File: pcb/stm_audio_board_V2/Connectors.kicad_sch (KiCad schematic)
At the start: 12 parts, among them J1 Power conn, J2 STlink, J3 Audio_sig, J4 Conn_01x10_display, J4 Conn_01x10_pots_internal, J5 SPI, J6 Conn_01x03_pot_ext, J6 Conn_01x03_taptempo

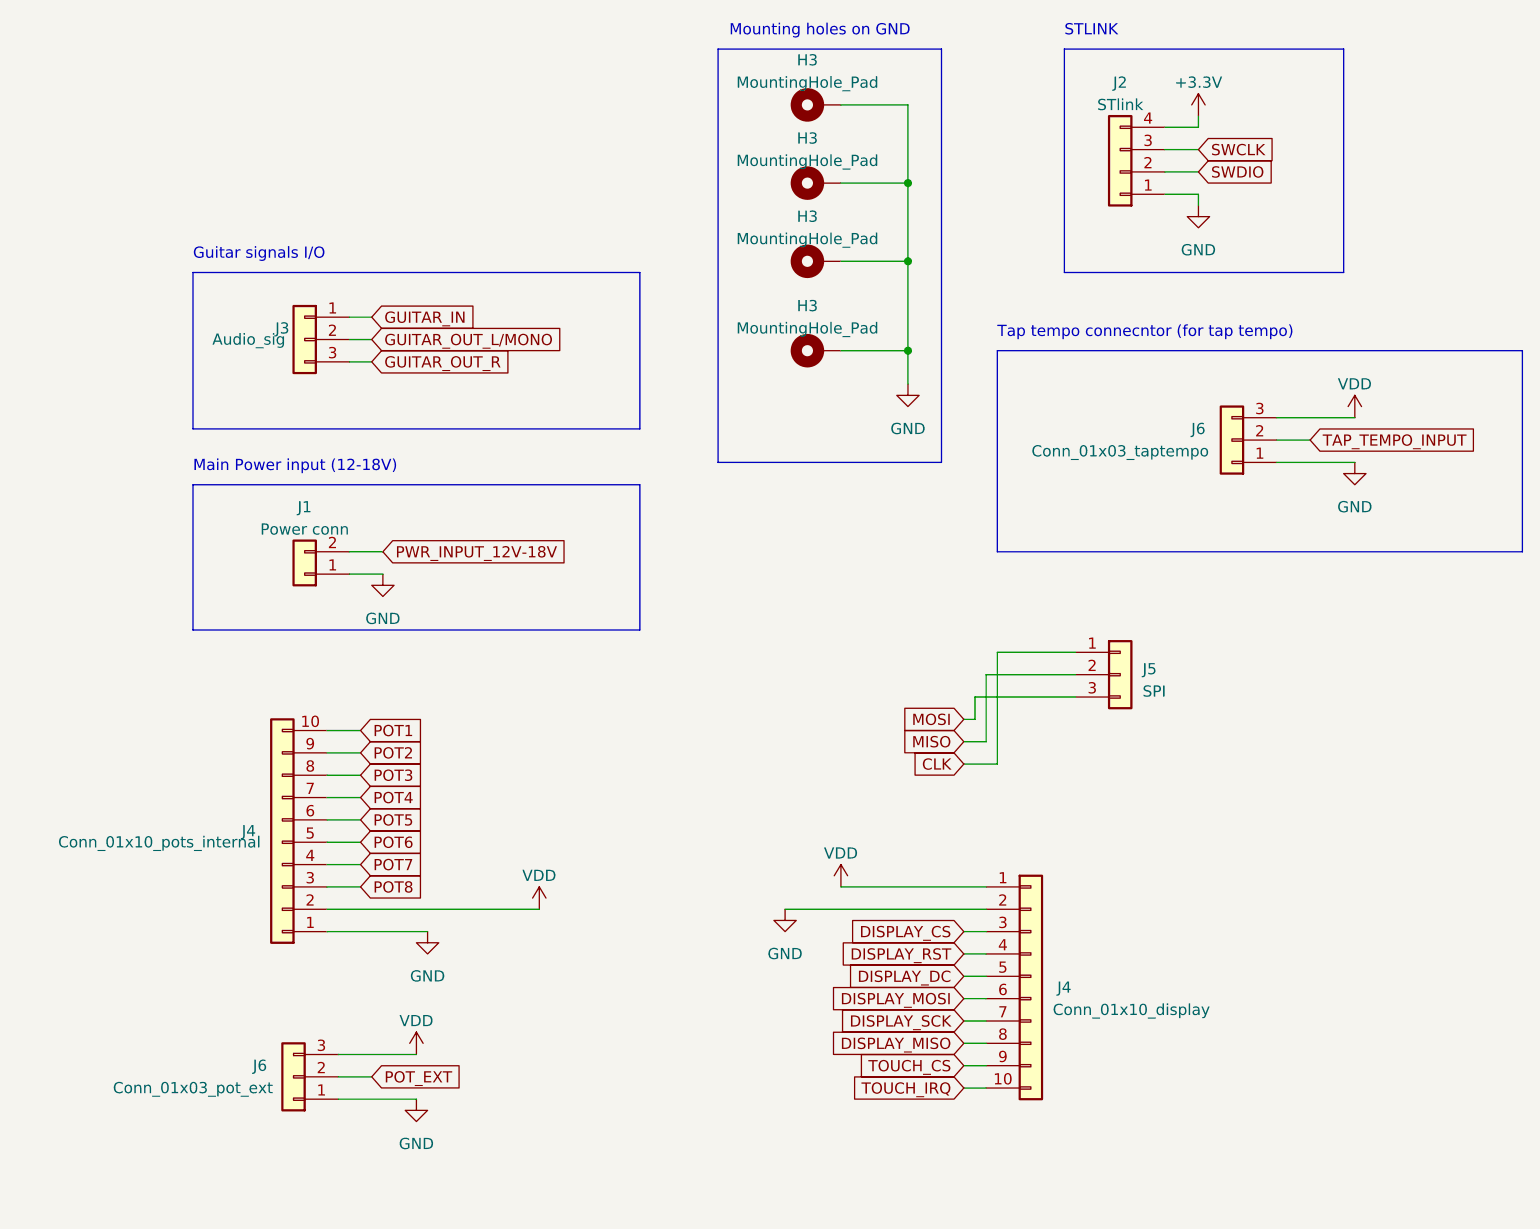
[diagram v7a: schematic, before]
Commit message: Capacitor types are choosen, schematic updated, unused capacitors deleted. Connectors need to be connected to the mcu and its finished
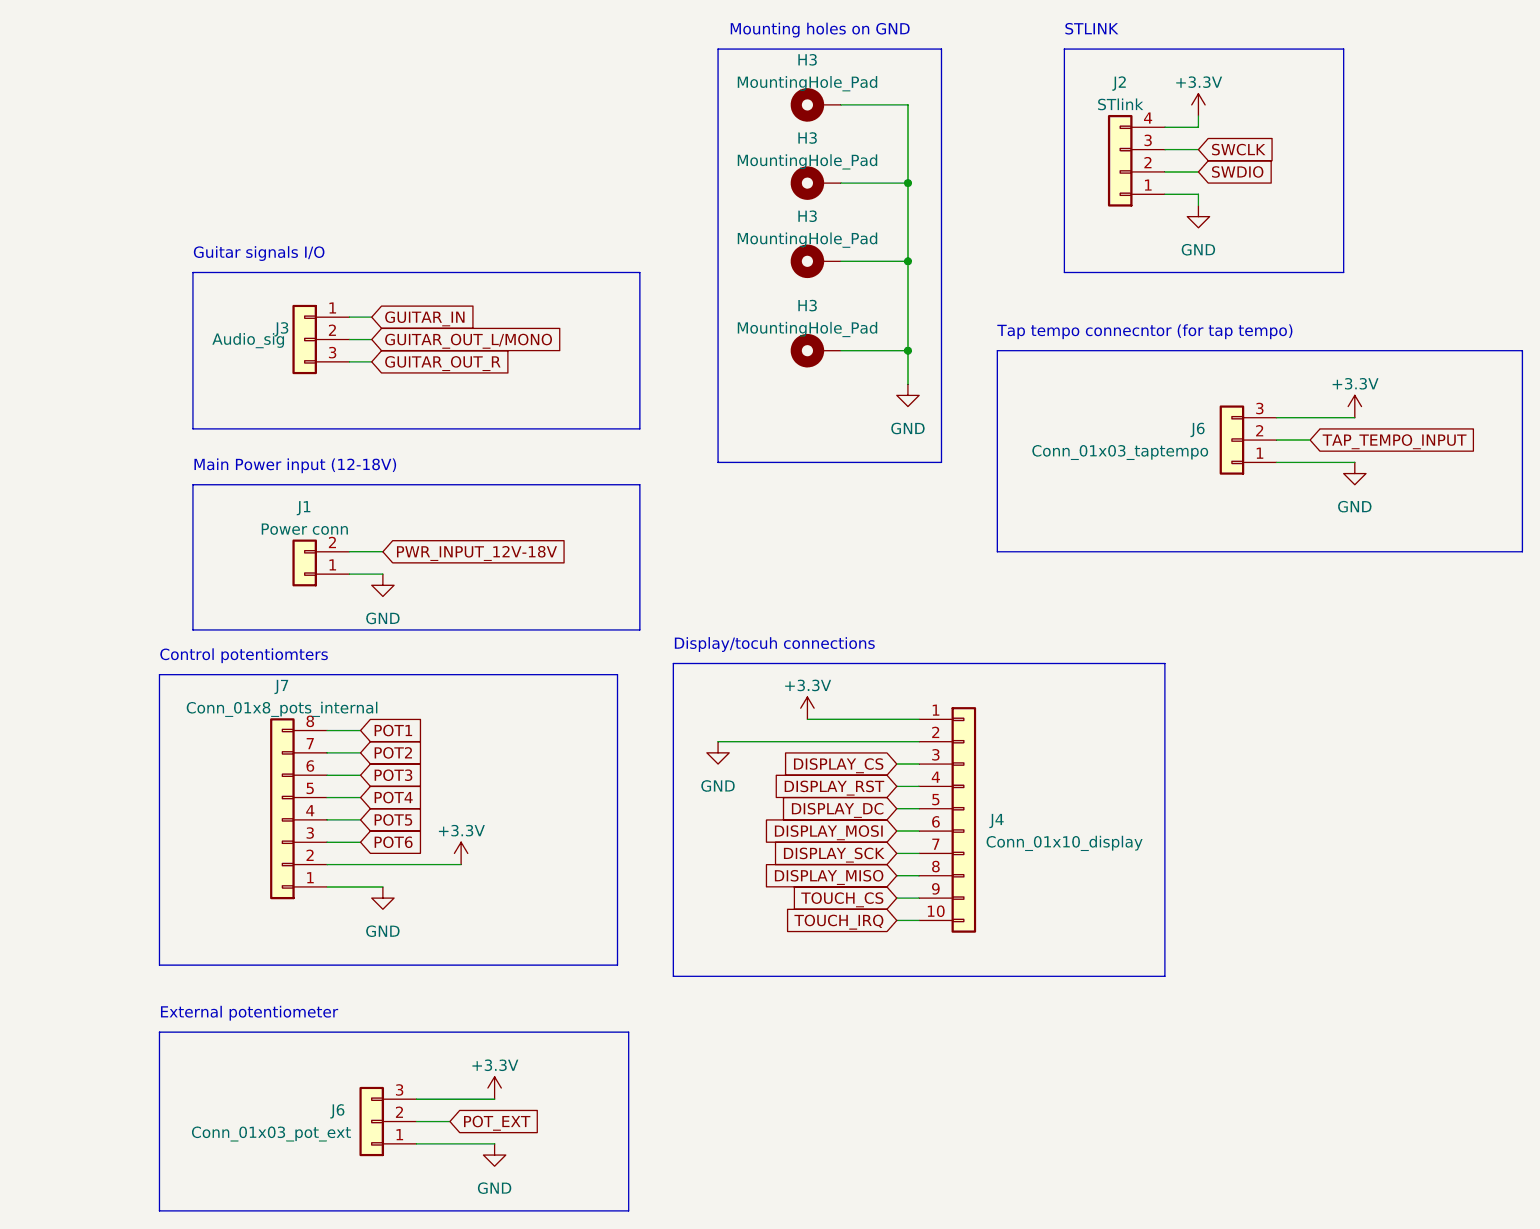
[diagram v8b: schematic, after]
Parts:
- removed J4: Conn_01x10_pots_internal, Connector_PinHeader_2.54mm:PinHeader_1x10_P2.54mm_Vertical, symbol Connector_Generic:Conn_01x10
- removed J5: SPI, Connector_PinHeader_2.54mm:PinHeader_1x03_P2.54mm_Vertical, symbol Connector_Generic:Conn_01x03
- added J7: Conn_01x8_pots_internal, Connector_PinHeader_2.54mm:PinHeader_1x08_P2.54mm_Vertical, symbol Connector_Generic:Conn_01x08
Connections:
- net VDD is gone; now on net +3.3V: J4.1 (Pin_1), J6.3 (Pin_3), J6.3 (Pin_3)
- net +3.3V: now also J7.2 (Pin_2)
- net GND: now also J7.1 (Pin_1)
- net POT1: now also J7.8 (Pin_8)
- net POT2: now also J7.7 (Pin_7)
- net POT3: now also J7.6 (Pin_6)
- net POT4: now also J7.5 (Pin_5)
- net POT5: now also J7.4 (Pin_4)
- net POT6: now also J7.3 (Pin_3)
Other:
- note added: "Control potentiomters"
- note added: "Display/tocuh connections"
- note added: "External potentiometer"
- moved on the sheet: J4, J6
